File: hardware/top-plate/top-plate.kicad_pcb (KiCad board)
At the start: 2 copper layers, 77.2 x 77.2 mm, 48 parts

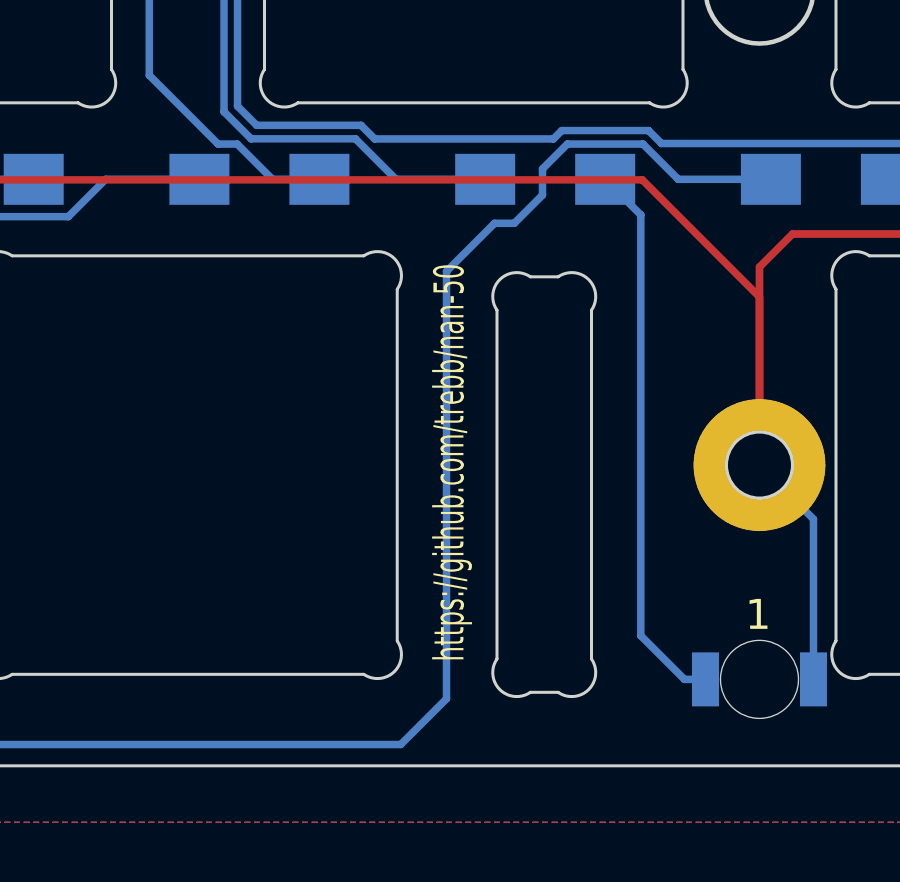
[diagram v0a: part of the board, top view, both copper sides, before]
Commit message: Design a bottom plate
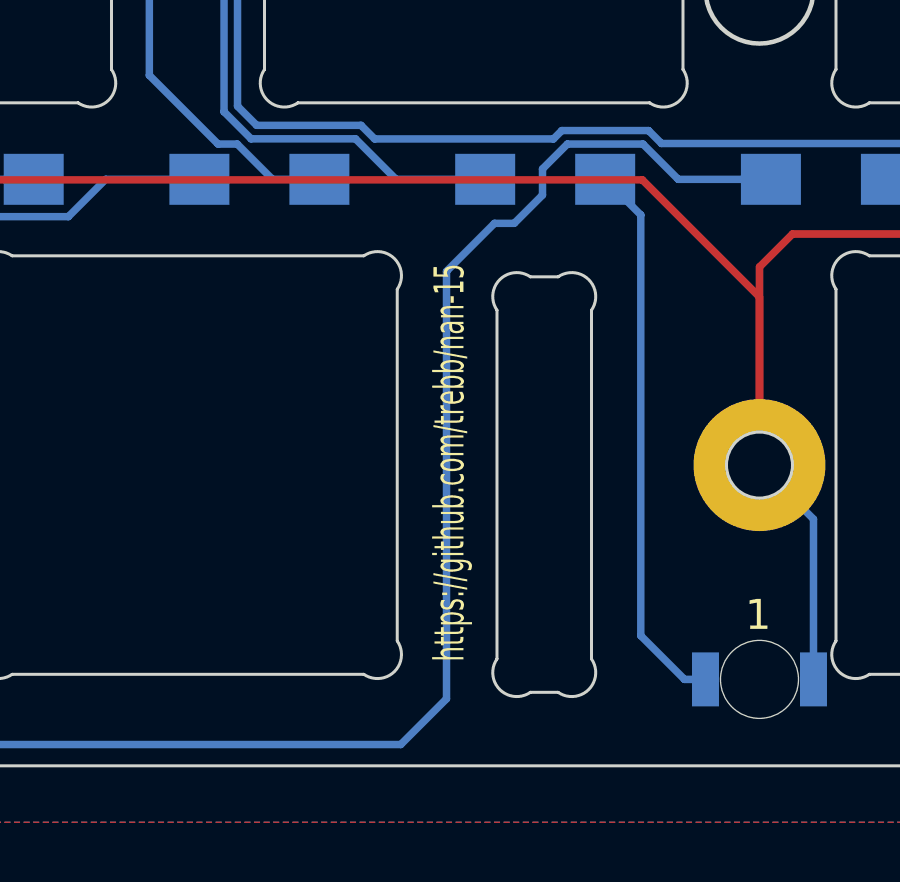
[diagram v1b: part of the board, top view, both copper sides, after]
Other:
- board text removed: "https://github.com/trebb/nan-50"
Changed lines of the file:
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@@
     (effects (font (size 3 5) (thickness 0.5)) (justify mirror))
   )
-  (gr_text https://github.com/trebb/nan-50 (at 153.3906 118.67515 90) (layer F.SilkS)
+  (gr_text https://github.com/trebb/nan-15 (at 153.3906 118.67515 90) (layer F.SilkS)
     (effects (font (size 1 0.6) (thickness 0.05)))
   )

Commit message: Connect all PWM pins to LEDs; show PCB version number
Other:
- board text added: "v0.1"
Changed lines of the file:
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@@
     (area 104.1908 49.70145 185.153301 130.663951)
     (thickness 1.6)
-    (drawings 169)
+    (drawings 170)
     (tracks 366)
     (zones 0)
@@
   (layers
     (0 F.Cu signal)
-    (31 B.Cu signal hide)
+    (31 B.Cu signal)
     (32 B.Adhes user)
     (33 F.Adhes user)
@@
     (35 F.Paste user)
     (36 B.SilkS user)
-    (37 F.SilkS user)
+    (37 F.SilkS user hide)
     (38 B.Mask user)
     (39 F.Mask user)
@@
       (net 14 /led0))
   )
-  (module Mounting_Holes:MountingHole_2.2mm_M2 (layer F.Cu)
+  (module Mounting_Holes:MountingHole_2.2mm_M2 locked (layer F.Cu)
     (at 130.38455 109.2327)
     (descr "Mounting Hole 2.2mm, no annular, M2")
@@
     (pad 1 np_thru_hole circle (at 0 0) (size 2.2 2.2) (drill 2.2) (layers *.Cu *.Mask F.SilkS))
   )
-  (module Mounting_Holes:MountingHole_2.2mm_M2 (layer F.Cu)
+  (module Mounting_Holes:MountingHole_2.2mm_M2 locked (layer F.Cu)
     (at 120.85955 109.2327)
     (descr "Mounting Hole 2.2mm, no annular, M2")
@@
     (pad 1 np_thru_hole circle (at 0 0) (size 2.2 2.2) (drill 2.2) (layers *.Cu *.Mask F.SilkS))
   )
-  (module Mounting_Holes:MountingHole_2.2mm_M2 (layer F.Cu)
+  (module Mounting_Holes:MountingHole_2.2mm_M2 locked (layer F.Cu)
     (at 130.38455 71.1327)
     (descr "Mounting Hole 2.2mm, no annular, M2")
@@
     (pad 1 np_thru_hole circle (at 0 0) (size 2.2 2.2) (drill 2.2) (layers *.Cu *.Mask F.SilkS))
   )
-  (module Mounting_Holes:MountingHole_2.2mm_M2 (layer F.Cu)
+  (module Mounting_Holes:MountingHole_2.2mm_M2 locked (layer F.Cu)
     (at 120.85955 71.1327)
     (descr "Mounting Hole 2.2mm, no annular, M2")
@@
       (net 2 GND))
   )
-  (module Symbols:OSHW-Logo_5.7x6mm_SilkScreen (layer B.Cu)
+  (module Symbols:OSHW-Logo_5.7x6mm_SilkScreen locked (layer B.Cu)
     (at 144.6784 81.41335 180)
     (descr "Open Source Hardware Logo")
@@
       (xy 0.376964 2.709982)) (layer B.SilkS) (width 0.01))
   )
+  (gr_text v0.1 (at 125.62205 111.61395 90) (layer B.SilkS)
+    (effects (font (size 1.5 1.5) (thickness 0.3)) (justify mirror))
+  )
   (gr_line (start 161.92205 96.5077) (end 161.92205 102.9077) (angle 90) (layer Edge.Cuts) (width 0.15))

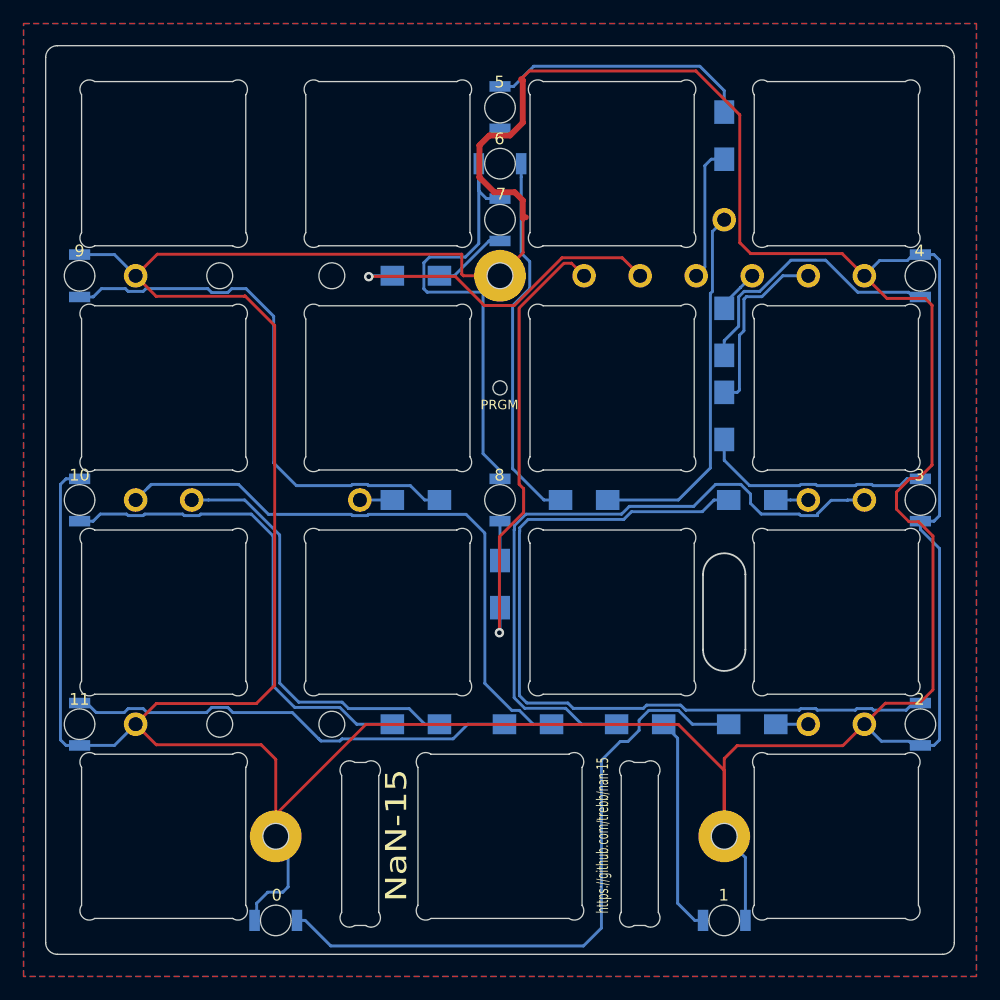
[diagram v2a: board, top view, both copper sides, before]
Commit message: Print switch numbers onto top plate
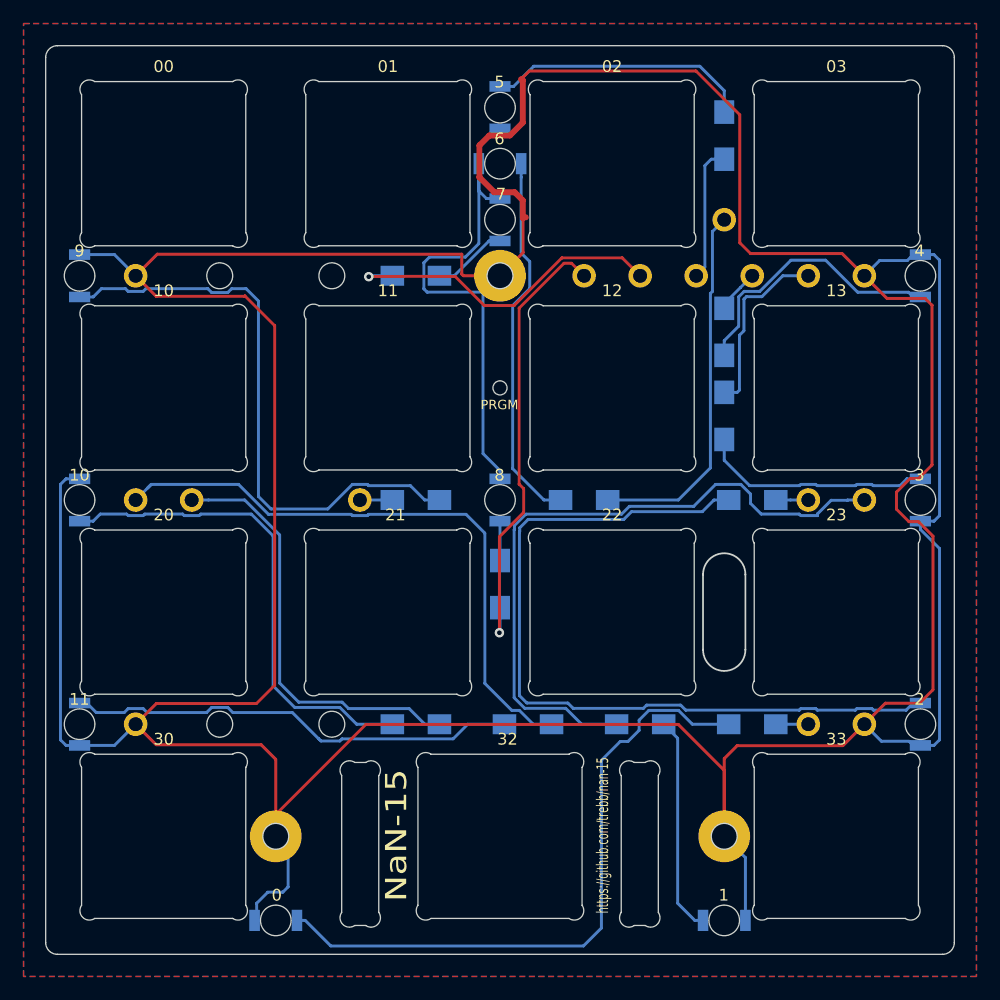
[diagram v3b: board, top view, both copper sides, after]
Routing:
- net Net-(D9-Pad2): track 46.2 -> 50.2 mm
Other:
- board text added: "00"
- board text added: "01"
- board text added: "02"
- board text added: "03"
- board text added: "12"
- board text added: "13"
- board text added: "20"
- board text added: "21"
- board text added: "22"
- board text added: "23"
- board text added: "30"
- board text added: "32"
- board text added: "33"
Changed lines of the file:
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@@
     (area 104.1908 49.70145 185.153301 130.663951)
     (thickness 1.6)
-    (drawings 170)
+    (drawings 185)
     (tracks 366)
     (zones 0)
@@
     (35 F.Paste user)
     (36 B.SilkS user)
-    (37 F.SilkS user hide)
+    (37 F.SilkS user)
     (38 B.Mask user)
     (39 F.Mask user)
@@
     (mod_text_size 1 1)
     (mod_text_width 0.15)
-    (pad_size 1.524 1.524)
-    (pad_drill 0.762)
+    (pad_size 4.4 4.4)
+    (pad_drill 2.2)
     (pad_to_mask_clearance 0.2)
     (aux_axis_origin 163.78555 118.7577)
@@
     (fp_circle (center 0 0) (end 2.45 0) (layer F.CrtYd) (width 0.05))
     (pad 1 thru_hole circle (at 0 0) (size 4.4 4.4) (drill 2.2) (layers *.Cu *.Mask F.SilkS)
-      (net 2 GND))
+      (net 2 GND) (zone_connect 2))
   )
   (module Mounting_Holes:MountingHole_2.2mm_M2_Pad (layer F.Cu)
@@
     (fp_circle (center 0 0) (end 2.45 0) (layer F.CrtYd) (width 0.05))
     (pad 1 thru_hole circle (at 0 0) (size 4.4 4.4) (drill 2.2) (layers *.Cu *.Mask F.SilkS)
-      (net 2 GND))
+      (net 2 GND) (zone_connect 2))
   )
   (module Mounting_Holes:MountingHole_2.2mm_M2_Pad (layer F.Cu)
@@
     (fp_circle (center 0 0) (end 2.45 0) (layer F.CrtYd) (width 0.05))
     (pad 1 thru_hole circle (at 0 0) (size 4.4 4.4) (drill 2.2) (layers *.Cu *.Mask F.SilkS)
-      (net 2 GND))
+      (net 2 GND) (zone_connect 2))
   )
   (module Symbols:OSHW-Logo_5.7x6mm_SilkScreen locked (layer B.Cu)
@@
       (xy -0.421237 2.40843) (xy -0.364389 2.709982) (xy -0.30754 3.011534) (xy 0.320115 3.011534)
       (xy 0.376964 2.709982)) (layer B.SilkS) (width 0.01))
+  )
+  (gr_text 30 (at 116.09705 110.5027) (layer F.SilkS)
+    (effects (font (size 1 1) (thickness 0.1)))
+  )
+  (gr_text 32 (at 145.30705 110.5027) (layer F.SilkS)
+    (effects (font (size 1 1) (thickness 0.1)))
+  )
+  (gr_text 33 (at 173.24705 110.5027) (layer F.SilkS)
+    (effects (font (size 1 1) (thickness 0.1)))
+  )
+  (gr_text 23 (at 173.24705 91.4527) (layer F.SilkS)
+    (effects (font (size 1 1) (thickness 0.1)))
+  )
+  (gr_text 22 (at 154.19705 91.4527) (layer F.SilkS)
+    (effects (font (size 1 1) (thickness 0.1)))
+  )
+  (gr_text 21 (at 135.78205 91.4527) (layer F.SilkS)
+    (effects (font (size 1 1) (thickness 0.1)))
+  )
+  (gr_text 20 (at 116.09705 91.4527) (layer F.SilkS)
+    (effects (font (size 1 1) (thickness 0.1)))
+  )
+  (gr_text 10 (at 116.09705 72.4027) (layer F.SilkS)
+    (effects (font (size 1 1) (thickness 0.1)))
+  )
+  (gr_text 11 (at 135.14705 72.4027) (layer F.SilkS)
+    (effects (font (size 1 1) (thickness 0.1)))
+  )
+  (gr_text 12 (at 154.19705 72.4027) (layer F.SilkS)
+    (effects (font (size 1 1) (thickness 0.1)))
+  )
+  (gr_text 13 (at 173.24705 72.4027) (layer F.SilkS)
+    (effects (font (size 1 1) (thickness 0.1)))
+  )
+  (gr_text 03 (at 173.24705 53.3527) (layer F.SilkS)
+    (effects (font (size 1 1) (thickness 0.1)))
+  )
+  (gr_text 02 (at 154.19705 53.3527) (layer F.SilkS)
+    (effects (font (size 1 1) (thickness 0.1)))
+  )
+  (gr_text 01 (at 135.14705 53.3527) (layer F.SilkS)
+    (effects (font (size 1 1) (thickness 0.1)))
+  )
+  (gr_text 00 (at 116.09705 53.3527) (layer F.SilkS)
+    (effects (font (size 1 1) (thickness 0.1)))
   )
   (gr_text v0.1 (at 125.62205 111.61395 90) (layer B.SilkS)
@@
   (segment (start 143.7408 68.1702) (end 144.67205 68.1702) (width 0.25) (layer B.Cu) (net 9))
   (segment (start 144.67205 95.32645) (end 144.67205 91.9827) (width 0.25) (layer B.Cu) (net 10))
-  (segment (start 127.37465 88.9635) (end 125.44425 87.0331) (width 0.25) (layer B.Cu) (net 11))
-  (segment (start 133.507602 88.9635) (end 133.401801 88.857699) (width 0.25) (layer B.Cu) (net 11))
+  (segment (start 124.14885 89.8779) (end 124.14885 73.279) (width 0.25) (layer B.Cu) (net 11))
   (segment (start 139.5283 90.1827) (end 138.2783 90.1827) (width 0.25) (layer B.Cu) (net 11))
-  (segment (start 110.10373 72.9327) (end 108.9533 72.9327) (width 0.25) (layer B.Cu) (net 11))
   (segment (start 138.2783 90.1827) (end 137.0591 88.9635) (width 0.25) (layer B.Cu) (net 11))
   (segment (start 137.0591 88.9635) (end 133.507602 88.9635) (width 0.25) (layer B.Cu) (net 11))
+  (segment (start 123.09475 72.2249) (end 121.876352 72.2249) (width 0.25) (layer B.Cu) (net 11))
+  (segment (start 114.584602 72.2249) (end 114.351801 72.457701) (width 0.25) (layer B.Cu) (net 11))
+  (segment (start 133.507602 88.9635) (end 133.401801 88.857699) (width 0.25) (layer B.Cu) (net 11))
+  (segment (start 121.543551 72.557701) (end 120.175549 72.557701) (width 0.25) (layer B.Cu) (net 11))
+  (segment (start 132.129799 88.857699) (end 130.042798 90.9447) (width 0.25) (layer B.Cu) (net 11))
   (segment (start 133.401801 88.857699) (end 132.129799 88.857699) (width 0.25) (layer B.Cu) (net 11))
+  (segment (start 114.351801 72.457701) (end 113.079799 72.457701) (width 0.25) (layer B.Cu) (net 11))
+  (segment (start 130.042798 90.9447) (end 125.21565 90.9447) (width 0.25) (layer B.Cu) (net 11))
+  (segment (start 125.21565 90.9447) (end 124.14885 89.8779) (width 0.25) (layer B.Cu) (net 11))
+  (segment (start 124.14885 73.279) (end 123.09475 72.2249) (width 0.25) (layer B.Cu) (net 11))
+  (segment (start 121.876352 72.2249) (end 121.543551 72.557701) (width 0.25) (layer B.Cu) (net 11))
+  (segment (start 119.842748 72.2249) (end 114.584602 72.2249) (width 0.25) (layer B.Cu) (net 11))
+  (segment (start 120.175549 72.557701) (end 119.842748 72.2249) (width 0.25) (layer B.Cu) (net 11))
+  (segment (start 110.10373 72.9327) (end 108.9533 72.9327) (width 0.25) (layer B.Cu) (net 11))
+  (segment (start 113.079799 72.457701) (end 112.846998 72.2249) (width 0.25) (layer B.Cu) (net 11))
   (segment (start 112.846998 72.2249) (end 110.81153 72.2249) (width 0.25) (layer B.Cu) (net 11))
-  (segment (start 119.842748 72.2249) (end 114.584602 72.2249) (width 0.25) (layer B.Cu) (net 11))
-  (segment (start 132.023998 88.9635) (end 127.37465 88.9635) (width 0.25) (layer B.Cu) (net 11))
-  (segment (start 132.129799 88.857699) (end 132.023998 88.9635) (width 0.25) (layer B.Cu) (net 11))
-  (segment (start 125.44425 87.0331) (end 125.44425 74.5744) (width 0.25) (layer B.Cu) (net 11))
-  (segment (start 121.876352 72.2249) (end 121.543551 72.557701) (width 0.25) (layer B.Cu) (net 11))
-  (segment (start 125.44425 74.5744) (end 123.09475 72.2249) (width 0.25) (layer B.Cu) (net 11))
-  (segment (start 121.543551 72.557701) (end 120.175549 72.557701) (width 0.25) (layer B.Cu) (net 11))
-  (segment (start 123.09475 72.2249) (end 121.876352 72.2249) (width 0.25) (layer B.Cu) (net 11))
-  (segment (start 120.175549 72.557701) (end 119.842748 72.2249) (width 0.25) (layer B.Cu) (net 11))
-  (segment (start 114.584602 72.2249) (end 114.351801 72.457701) (width 0.25) (layer B.Cu) (net 11))
-  (segment (start 113.079799 72.457701) (end 112.846998 72.2249) (width 0.25) (layer B.Cu) (net 11))
-  (segment (start 114.351801 72.457701) (end 113.079799 72.457701) (width 0.25) (layer B.Cu) (net 11))
   (segment (start 110.81153 72.2249) (end 110.10373 72.9327) (width 0.25) (layer B.Cu) (net 11))
   (segment (start 127.233759 107.807699) (end 125.3998 105.97374) (width 0.25) (layer B.Cu) (net 12))
